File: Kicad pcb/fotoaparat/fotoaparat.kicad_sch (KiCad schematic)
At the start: 8 parts, among them J1 USB Konektor, J3 LCD konektor, J4 Kamera, J5 Sd Karta, U1 STM32L496RETx, U2 Regulator 3.3v, U3 MCP73833-FCI/UN

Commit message: První zapojení
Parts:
- added R1, R2: MCU08050D1002BP500, RESC2012X55N, symbol MCU08050D1002BP500:MCU08050D1002BP500
- added S2, S3, S4: MC32829, MC32829, symbol MC32829:MC32829
- added S5: CFS-0201MB, CFS0201MB, symbol CFS-0201MB:CFS-0201MB
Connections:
- net at U1.18 (VSS), U1.31 (VSS), U1.47 (VSS)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: now also R1.1, S5.B2 (NO_2)
- net at U1.60 (PH3): now also R1.2, S5.A1 (COM_1)
- net at U1.64 (VDD): now also R2.1, S5.B1 (NO_1)
- net at U1.7 (NRST): now also R2.2, S5.A2 (COM_2)

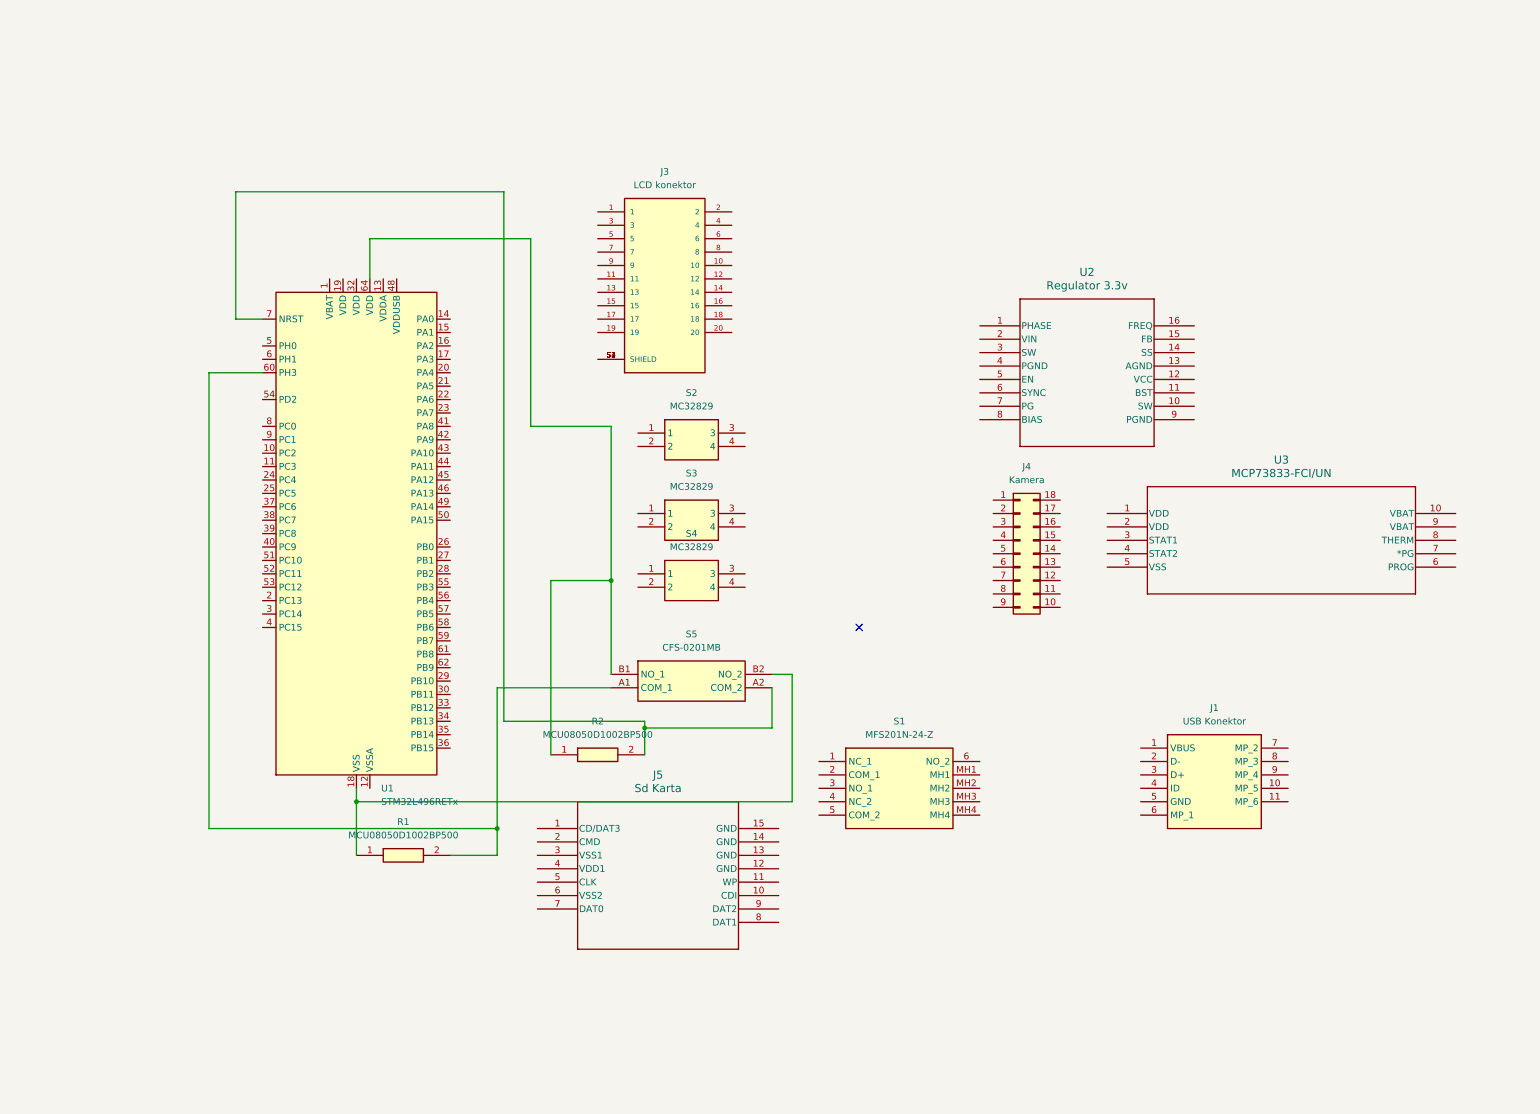
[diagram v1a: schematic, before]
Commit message: Zapojení kamery tlačítek debug pinů atd
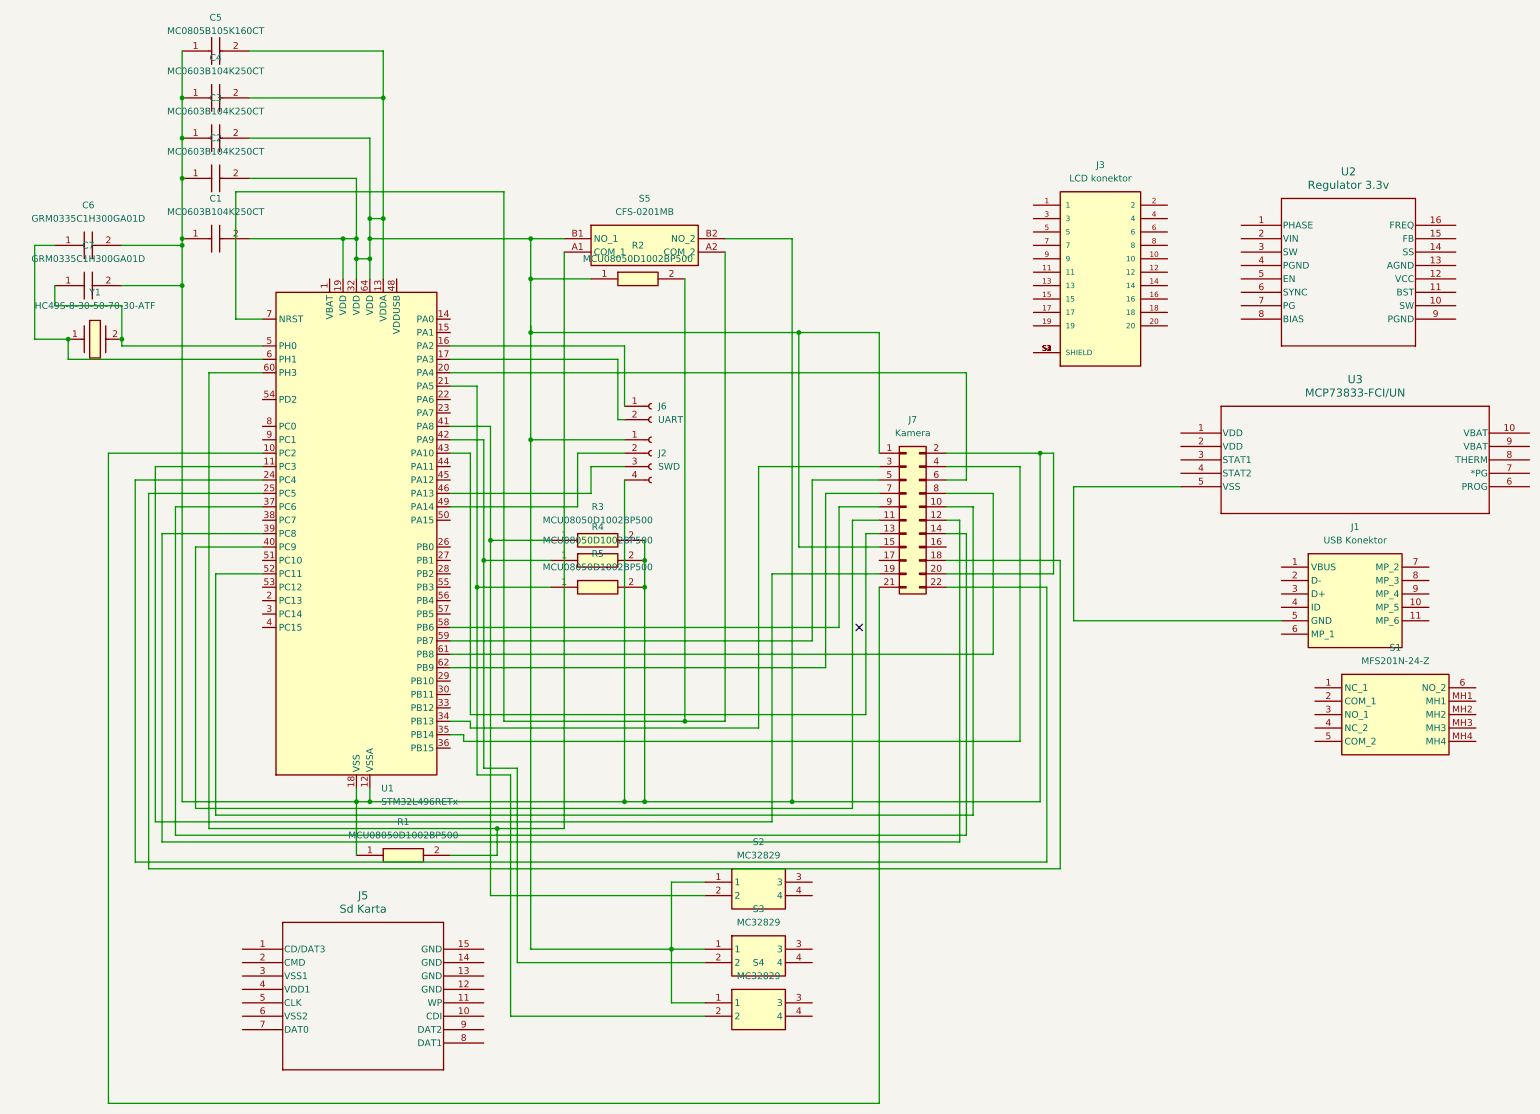
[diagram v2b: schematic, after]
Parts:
- removed J4: Kamera, Connector_PinHeader_2.54mm:PinHeader_2x09_P2.54mm_Vertical_SMD, symbol Connector_Generic:Conn_02x09_Counter_Clockwise
- added C1, C2, C3, C4: MC0603B104K250CT, mc06:CAPC1608X87N, symbol MC0603B104K250CT:MC0603B104K250CT
- added C5: MC0805B105K160CT, mc08:CAPC2012X135N, symbol MC0805B105K160CT:MC0805B105K160CT
- added C6, C7: GRM0335C1H300GA01D, grm033:GRM033D70J224ME01D, symbol GRM0335C1H300GA01D:GRM0335C1H300GA01D
- added J2: SWD, Connector_PinSocket_2.54mm:PinSocket_1x04_P2.54mm_Vertical, symbol Connector:Conn_01x04_Socket
- added J6: UART, Connector_PinSocket_2.54mm:PinSocket_1x02_P2.54mm_Vertical, symbol Connector:Conn_01x02_Socket
- added J7: Kamera, Connector_PinHeader_2.54mm:PinHeader_2x11_P2.54mm_Vertical, symbol Connector_Generic:Conn_02x11_Odd_Even
- added R3, R4, R5: MCU08050D1002BP500, 2012:RESC2012X55N, symbol MCU08050D1002BP500:MCU08050D1002BP500
- added Y1: HC49S-8-30-50-70-30-ATF, hc4:HC49S830507030ATF, symbol HC49S-8-30-50-70-30-ATF:HC49S-8-30-50-70-30-ATF
- J1: footprint 473460001 -> 47436:473460001
- J5: footprint GSD090012SEU_AMP -> gsd09:GSD090012SEU_AMP
- R1, R2: footprint RESC2012X55N -> 2012:RESC2012X55N
- S1: footprint MFS201N24Z -> mfs:MFS201N24Z
- S2, S3, S4: footprint MC32829 -> mc3:MC32829
- S5: footprint CFS0201MB -> cfs:CFS0201MB
- U2: footprint QFN-3x4_MPQ4432_MNP -> MPQ:QFN-3x4_MPQ4432_MNP
- U3: footprint MSOP10_MC_MCH -> MCP:MSOP10_MC_MCH
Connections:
- net at U1.10 (PC2): now also J7.21 (Pin_21)
- net at U1.11 (PC3): now also J7.19 (Pin_19)
- net at U1.12 (VSSA): now also R1.1, S5.B2 (NO_2), U1.18 (VSS), U1.31 (VSS), U1.47 (VSS), U1.63 (VSS), C1.1, C2.1, C3.1, C4.1, C5.1, C6.2, C7.2, J2.4 (Pin_4), J7.2 (Pin_2), J7.20 (Pin_20), R3.2, R4.2, R5.2
- net at U1.13 (VDDA): now also R2.1, S2.1, S3.1, S4.1, S5.B1 (NO_1), U1.19 (VDD), U1.32 (VDD), U1.64 (VDD), C1.2, C2.2, C3.2, C4.2, C5.2, J2.1 (Pin_1), J7.1 (Pin_1), J7.15 (Pin_15)
- net at U1.16 (PA2): now also J6.1 (Pin_1)
- net at U1.17 (PA3): now also J6.2 (Pin_2)
- net at U1.20 (PA4): now also J7.6 (Pin_6)
- net at U1.21 (PA5): now also S4.2, R5.1
- net at U1.24 (PC4): now also J7.22 (Pin_22)
- net at U1.25 (PC5): now also J7.18 (Pin_18)
- net at U1.34 (PB13): now also J7.3 (Pin_3)
- net at U1.35 (PB14): now also J7.4 (Pin_4)
- net at U1.37 (PC6): now also J7.14 (Pin_14)
- net at U1.39 (PC8): now also J7.12 (Pin_12)
- net at U1.40 (PC9): now also J7.11 (Pin_11)
- net at U1.41 (PA8): now also S2.2, R3.1
- net at U1.42 (PA9): now also S3.2, R4.1
- net at U1.43 (PA10): now also J7.13 (Pin_13)
- net at U1.46 (PA13): now also J2.3 (Pin_3)
- net at U1.49 (PA14): now also J2.2 (Pin_2)
- net at U1.5 (PH0): now also C7.1, Y1.2
- net at U1.52 (PC11): now also J7.10 (Pin_10)
- net at U1.58 (PB6): now also J7.9 (Pin_9)
- net at U1.59 (PB7): now also J7.5 (Pin_5)
- net at U1.6 (PH1): now also C6.1, Y1.1
- net at U1.61 (PB8): now also J7.8 (Pin_8)
- net at U1.62 (PB9): now also J7.7 (Pin_7)
- net at U3.5 (VSS): now also J1.5 (GND)
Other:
- moved on the sheet: J1, J3, J5, R2, S1, S2, S3, S4, S5, U2, U3

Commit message: Lcd Konektor
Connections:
- net at C1.2, C2.2, C3.2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: now also J3.2, J3.5
- net at C1.1, C2.1, C3.1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: now also J3.1, J3.11, J3.20, J3.3, J3.4
- net at U1.15 (PA1): now also J3.8
- net at U1.22 (PA6): now also J3.12
- net at U1.23 (PA7): now also J3.7

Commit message: Baterie
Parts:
- added C8: MC0603B104K250CT, mc06:CAPC1608X87N, symbol MC0603B104K250CT:MC0603B104K250CT
- added J4: Baterie, symbol Connector:Conn_01x02_Socket
- added R10, R6, R7, R8, R9: MCU08050D1002BP500, 2012:RESC2012X55N, symbol MCU08050D1002BP500:MCU08050D1002BP500
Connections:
- net at S1.MH1: now also C1.1, C2.1, C3.1, C4.1, C5.1, C6.2, C7.2, J1.10 (MP_5), J1.11 (MP_6), J1.5 (GND), J1.6 (MP_1), J1.7 (MP_2), J1.8 (MP_3), J1.9 (MP_4), J2.4 (Pin_4), J3.1, J3.11, J3.15, J3.20, J3.3, J3.4, J3.S1 (SHIELD), J3.S2 (SHIELD), J3.S3 (SHIELD), J3.S4 (SHIELD), J5.12 (GND), J5.13 (GND), J5.14 (GND), J5.15 (GND), J5.3 (VSS1), J5.6 (VSS2), J7.2 (Pin_2), J7.20 (Pin_20), R1.1, R3.2, R4.2, R5.2, S1.MH2, S1.MH3, S1.MH4, S5.B2 (NO_2), U1.12 (VSSA), U1.18 (VSS), U1.31 (VSS), U1.47 (VSS), U1.63 (VSS), U3.5 (VSS), C8.2, J4.1 (Pin_1), R10.1
- net at C1.2, C2.2, C3.2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: now also J3.14, J5.4 (VDD1), C8.1, R6.1, R7.1, R8.1
- net at J7.21 (Pin_21): now also U1.9 (PC1); no longer U1.10 (PC2)
- net at U1.26 (PB0): now also J3.9
- net at U1.27 (PB1): now also J3.10
- net at U1.29 (PB10): now also J5.5 (CLK)
- net at U1.33 (PB12): now also J5.1 (CD/DAT3), R1.2, S5.A1 (COM_1), U1.60 (PH3), R6.2
- net at U1.36 (PB15): now also J5.2 (CMD), R8.2
- net at U1.44 (PA11): now also J3.6
- net at U1.8 (PC0): now also R10.2, R9.1
- net at J5.7 (DAT0): now also U1.10 (PC2), R7.2
- net at U3.10 (VBAT): now also J4.2 (Pin_2), R9.2
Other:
- moved on the sheet: J1, S1, U2, U3

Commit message: Přepojení součástek
vypadá to trochu lépe
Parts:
- removed C1, C2, C3, C4, C8: MC0603B104K250CT, mc06:CAPC1608X87N, symbol MC0603B104K250CT:MC0603B104K250CT
- removed C5: MC0805B105K160CT, mc08:CAPC2012X135N, symbol MC0805B105K160CT:MC0805B105K160CT
- removed C6, C7: GRM0335C1H300GA01D, grm033:GRM033D70J224ME01D, symbol GRM0335C1H300GA01D:GRM0335C1H300GA01D
- removed R1, R10, R2, R3, R4, R5, R6, R7, R8, R9: MCU08050D1002BP500, 2012:RESC2012X55N, symbol MCU08050D1002BP500:MCU08050D1002BP500
- removed U2: Regulator 3.3v, MPQ:QFN-3x4_MPQ4432_MNP, symbol 2025-09-30_17-10-32:MPQ4432GL-AEC1-P
- added C10, C11, C12, C9: 100n, Capacitor_SMD:C_0603_1608Metric_Pad1.08x0.95mm_HandSolder, symbol Device:C
- added C13: 5u, symbol Device:C
- added C14: 10n, Capacitor_SMD:C_0603_1608Metric_Pad1.08x0.95mm_HandSolder, symbol Device:C
- added C15, C16: 1u, symbol Device:C
- added C17, C18: 30p, Capacitor_SMD:C_0201_0603Metric_Pad0.64x0.40mm_HandSolder, symbol Device:C
- added FB1: 120R, symbol Device:FerriteBead
- added IC1: NCP718ASN330T1G, SOT95P280X100-5N, symbol NCP718ASN330T1G:NCP718ASN330T1G
- added R1, R11, R12, R13, R2, R3: 1.5k, symbol Device:R
- S2: value MC32829 -> tlačítko doleva
- S3: value MC32829 -> prostřední tlačítko
- S4: value MC32829 -> tlačítko doprava
- S5: value CFS-0201MB -> spínač
- Y1: value HC49S-8-30-50-70-30-ATF -> 8mhz krystal
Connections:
- net at J4.2 (Pin_2): no longer U3.10 (VBAT)
- net +3.3V: now reaches J2.1 (Pin_1), J3.2, J3.5, J7.1 (Pin_1), J7.15 (Pin_15), U1.19 (VDD), U1.32 (VDD), U1.64 (VDD)
- net +3.3V: now also J5.3 (VSS1), J5.6 (VSS2), S5.A2 (COM_2), U1.1 (VBAT), C10.2, C11.2, C12.2, C13.2, C16.1, C9.2, FB1.2, R1.1, R11.1, R13.2, R2.1, R3.1; no longer J3.14, J5.4 (VDD1), S2.1, S3.1, S4.1, S5.B1 (NO_1), U1.13 (VDDA)
- net d4: now reaches J7.10 (Pin_10), U1.52 (PC11)
- net d3: now reaches J7.11 (Pin_11), U1.40 (PC9)
- net d2: now reaches J7.12 (Pin_12), U1.39 (PC8)
- net at U1.43 (PA10): no longer J7.13 (Pin_13)
- net d0: now reaches J7.14 (Pin_14), U1.37 (PC6)
- net rck: now reaches J7.18 (Pin_18)
- net rck: now also U1.53 (PC12); no longer U1.25 (PC5)
- net sw1: now reaches U1.11 (PC3)
- net sw1: now also S2.4, R3.2; no longer J7.19 (Pin_19)
- net sda: now reaches U1.9 (PC1)
- net sda: now also J3.7, J7.4 (Pin_4), U1.30 (PB11); no longer J7.21 (Pin_21)
- net rrst: now reaches J7.22 (Pin_22)
- net rrst: now also U1.2 (PC13); no longer U1.24 (PC4)
- net scl: now reaches J7.3 (Pin_3), U1.34 (PB13)
- net scl: now also J3.8, U1.29 (PB10)
- net at U1.35 (PB14): no longer J7.4 (Pin_4)
- net vsync: now reaches J7.5 (Pin_5), U1.59 (PB7)
- net href: now reaches J7.6 (Pin_6), U1.20 (PA4)
- net d7: now reaches J7.7 (Pin_7), U1.62 (PB9)
- net d6: now reaches J7.8 (Pin_8), U1.61 (PB8)
- net d5: now reaches J7.9 (Pin_9), U1.58 (PB6)
- net sd miso: now reaches J5.7 (DAT0)
- net sd miso: now also U1.56 (PB4); no longer U1.10 (PC2)
- net uart tx: now reaches U1.14 (PA0)
- net uart tx: now also J6.1 (Pin_1)
- net uart rx: now reaches U1.15 (PA1)
- net uart rx: now also J6.2 (Pin_2); no longer J3.8
- net at U1.16 (PA2): no longer J6.1 (Pin_1)
- net sd cs: now reaches U1.17 (PA3)
- net sd cs: now also J5.1 (CD/DAT3); no longer J6.2 (Pin_2)
- net at S4.2: no longer U1.21 (PA5)
- net sdo: now reaches J3.12
- net sdo: now also U1.10 (PC2); no longer U1.22 (PA6)
- net sd mosi: now reaches U1.23 (PA7)
- net sd mosi: now also J5.2 (CMD); no longer J3.7
- net at U1.26 (PB0): no longer J3.9
- net at U1.27 (PB1): no longer J3.10
- net sd clk: now reaches J5.5 (CLK)
- net sd clk: now also U1.21 (PA5); no longer U1.29 (PB10)
- net wrst: now reaches U1.3 (PC14)
- net wrst: now also J7.21 (Pin_21)
- net at U1.36 (PB15): no longer J5.2 (CMD)
- net d1: now reaches U1.38 (PC7)
- net d1: now also J7.13 (Pin_13)
- net at U1.41 (PA8): no longer S2.2
- net at U1.42 (PA9): no longer S3.2
- net at J3.6: no longer U1.44 (PA11)
- net data +: now reaches U1.45 (PA12)
- net data +: now also J1.3 (D+)
- net swclk: now reaches J2.3 (Pin_3)
- net swclk: now also U1.49 (PA14); no longer U1.46 (PA13)
- net +3.3VA: now reaches U1.48 (VDDUSB)
- net +3.3VA: now also C14.1, C15.1, FB1.1
- net swdio: now reaches J2.2 (Pin_2)
- net swdio: now also U1.46 (PA13); no longer U1.49 (PA14)
- net osc in: now reaches U1.5 (PH0)
- net osc in: now also Y1.1, C17.2; no longer Y1.2
- net osc out: now reaches U1.6 (PH1)
- net osc out: now also Y1.2, C18.2; no longer Y1.1
- net Reset: now reaches U1.7 (NRST)
- net Reset: now also S5.A1 (COM_1), R11.2; no longer S5.A2 (COM_2)
- net GND: now reaches S4.3
- net GND: now also J1.5 (GND), J2.4 (Pin_4), J3.1, J3.11, J3.15, J3.20, J3.3, J3.4, J5.4 (VDD1), J7.2 (Pin_2), J7.20 (Pin_20), S2.3, S3.3, S5.B1 (NO_1), U1.12 (VSSA), U1.18 (VSS), U1.31 (VSS), U1.47 (VSS), U1.63 (VSS), C10.1, C11.1, C12.1, C13.1, C14.2, C15.2, C16.2, C17.1, C18.1, C9.1, R12.1
- net sw3: now reaches S4.4
- net sw3: now also U1.25 (PC5), R1.2
- net sw2: now reaches S3.4
- net sw2: now also U1.24 (PC4), R2.2
- net VBUS: now reaches J1.1 (VBUS)
- net data -: now reaches J1.2 (D-)
- net data -: now also U1.44 (PA11)
- new net: J3.14, R13.1
- new net: J3.S1 (SHIELD), J3.S2 (SHIELD), J3.S3 (SHIELD), J3.S4 (SHIELD)
- new net boot0: R12.2, S5.B2 (NO_2), U1.60 (PH3)
- new net wr: J7.19 (Pin_19), U1.22 (PA6)
- now unconnected: J1.10 (MP_5), J1.11 (MP_6), J1.6 (MP_1), J1.7 (MP_2), J1.8 (MP_3), J1.9 (MP_4), J4.1 (Pin_1), J5.12 (GND), J5.13 (GND), J5.14 (GND), J5.15 (GND), S1.MH1, S1.MH2, S1.MH3, S1.MH4, U1.33 (PB12), U3.5 (VSS)
- no-connect marks 1 -> 29
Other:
- moved on the sheet: J1, J2, J3, J4, J5, J6, J7, S1, S2, S3, S4, S5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

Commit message: Baterie nabíječka
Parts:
- added C1, C2: 1u, symbol Device:C
- added D1, D2, D3: LED, symbol Device:LED
- added R4, R5, R6: 1.5k, symbol Device:R
- added R7: 1k, symbol Device:R
- added TH1: 10k, symbol Device:Thermistor
- IC1: value NCP718ASN330T1G -> Lineární Regulátor
- S1: value MFS201N-24-Z -> Zapínací spínač
- U3: value MCP73833-FCI/UN -> Nabíječka baterie
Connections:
- net GND is gone; now on net -BATT: C10.1, C11.1, C12.1, C13.1, C14.2, C15.2, C16.2, C17.1, C18.1, C9.1, J1.5 (GND), J2.4 (Pin_4), J3.1, J3.11, J3.15, J3.20, J3.3, J3.4, J5.4 (VDD1), J7.2 (Pin_2), J7.20 (Pin_20), R12.1, S2.3, S3.3, S4.3, S5.B1 (NO_1), U1.12 (VSSA), U1.18 (VSS), U1.31 (VSS), U1.47 (VSS), U1.63 (VSS)
- net VBUS: now also U3.1 (VDD), U3.2 (VDD), C1.1, D1.2 (A), D2.2 (A), D3.2 (A)
- net +BATT: now reaches J4.1 (Pin_1)
- net +BATT: now also U3.10 (VBAT), U3.9 (VBAT), C2.1
- net -BATT: now reaches J4.2 (Pin_2)
- net -BATT: now also U3.5 (VSS), C1.2, C2.2, R7.2, TH1.2
- net at U3.3 (STAT1): now also R4.2
- net at U3.4 (STAT2): now also R5.2
- net at U3.6 (PROG): now also R7.1
- net at U3.7 (*PG): now also R6.2
- net at U3.8 (THERM): now also TH1.1
- new net: D2.1 (K), R5.1
- new net: D1.1 (K), R4.1
- new net Indikátor Nabíjení: D3.1 (K), R6.1
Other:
- moved on the sheet: IC1, J4, S1, U3

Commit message: Regulátory
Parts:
- added C19, C20, C3, C4, C5, C6, C7, C8: 1u, Capacitor_SMD:C_0805_2012Metric_Pad1.18x1.45mm_HandSolder, symbol Device:C
- added IC2: Lineární Regulátor Displaye, Package_TO_SOT_SMD:TSOT-23-5_HandSoldering, symbol NCP718ASN330T1G:NCP718ASN330T1G
- added R10, R14, R15, R16, R17, R18, R19, R20, R21, R22, R23, R24, R9: 4.7k, Resistor_SMD:R_0805_2012Metric_Pad1.20x1.40mm_HandSolder, symbol Device:R
- added R8: 2, Resistor_SMD:R_0805_2012Metric_Pad1.20x1.40mm_HandSolder, symbol Device:R
- C1, C15, C16, C2: footprint (none) -> Capacitor_SMD:C_0805_2012Metric_Pad1.18x1.45mm_HandSolder
- C10, C11, C12, C9: footprint Capacitor_SMD:C_0603_1608Metric_Pad1.08x0.95mm_HandSolder -> Capacitor_SMD:C_0805_2012Metric_Pad1.18x1.45mm_HandSolder
- C13: value 5u -> 1u; footprint (none) -> Capacitor_SMD:C_0805_2012Metric_Pad1.18x1.45mm_HandSolder
- C14: value 10n -> 100n; footprint Capacitor_SMD:C_0603_1608Metric_Pad1.08x0.95mm_HandSolder -> Capacitor_SMD:C_0805_2012Metric_Pad1.18x1.45mm_HandSolder
- C17, C18: footprint Capacitor_SMD:C_0201_0603Metric_Pad0.64x0.40mm_HandSolder -> Capacitor_SMD:C_0805_2012Metric_Pad1.18x1.45mm_HandSolder
- D1, D2, D3: footprint (none) -> LED_SMD:LED_0805_2012Metric_Pad1.15x1.40mm_HandSolder
- FB1: footprint (none) -> Inductor_SMD:L_0805_2012Metric_Pad1.05x1.20mm_HandSolder
- IC1: footprint SOT95P280X100-5N -> Package_TO_SOT_SMD:TSOT-23-5_HandSoldering
- J2: footprint Connector_PinSocket_2.54mm:PinSocket_1x04_P2.54mm_Vertical -> Connector_PinHeader_2.54mm:PinHeader_1x04_P2.54mm_Vertical
- J4, TH1: footprint (none) -> Connector_PinSocket_2.54mm:PinSocket_1x02_P2.54mm_Horizontal
- J6: footprint Connector_PinSocket_2.54mm:PinSocket_1x02_P2.54mm_Vertical -> Connector_PinHeader_2.54mm:PinHeader_1x02_P2.54mm_Vertical
- J7: footprint Connector_PinHeader_2.54mm:PinHeader_2x11_P2.54mm_Vertical -> Connector_PinSocket_2.54mm:PinSocket_2x11_P2.54mm_Vertical
- R1, R11, R12, R13, R2, R3: value 1.5k -> 4.7k; footprint (none) -> Resistor_SMD:R_0805_2012Metric_Pad1.20x1.40mm_HandSolder
- R4, R5, R6: value 1.5k -> 1k; footprint (none) -> Resistor_SMD:R_0805_2012Metric_Pad1.20x1.40mm_HandSolder
- R7: footprint (none) -> Resistor_SMD:R_0805_2012Metric_Pad1.20x1.40mm_HandSolder
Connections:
- net +3.3V: now also IC1.5 (OUT), C19.2, C20.2, C4.2, C7.2, C8.2, R10.1, R15.1, R18.1, R21.1, R9.1; no longer J3.2, J3.5, R13.2
- net +BATT: now also IC1.1 (IN), S1.2 (COM_1), C3.1, C5.1, IC2.1 (IN)
- net -BATT: now also IC1.2 (GND), C19.1, C20.1, C3.2, C4.1, C5.2, C6.1, C7.1, C8.1, IC2.2 (GND), R14.1, R24.1
- net scl: now also R9.2
- net sd cs: now also R17.2
- net sd miso: now also R23.2
- net sd mosi: now also R20.2
- net sdo: now also J7.4 (Pin_4), U1.30 (PB11), R10.2
- net at S1.3 (NO_1): now also IC1.3 (EN), R24.2
- net Backlight Regulátor: now reaches S1.5 (COM_2)
- net Backlight Regulátor: now also U1.4 (PC15)
- net at S1.6 (NO_2): now also IC2.3 (EN), R14.2
- net rst: now reaches U1.28 (PB2)
- net rst: now also J3.6
- net csx: now reaches U1.55 (PB3)
- net csx: now also J3.7, J3.9, U1.9 (PC1)
- net wrx d/cx: now reaches U1.57 (PB5)
- net wrx d/cx: now also J3.10
- net data + renamed USB_D+
- net data - renamed USB_D-
- removed net sda: J3.7, J7.4 (Pin_4), U1.30 (PB11), U1.9 (PC1)
- new net: R18.2, R19.1
- new net: R15.2, R16.1
- new net: R19.2, R20.1
- new net: J3.2, R8.2
- new net: R21.2, R22.1
- new net: R22.2, R23.1
- new net: R16.2, R17.1
- new net +3.3V LCD: C6.2, IC2.5 (OUT), J3.5, R13.2, R8.1
- no-connect marks 29 -> 37
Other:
- note added: "Regulátory"
- note added: "Stm32 mikrokontrolér"
- company: (none) -> Vilem Maly
- title: (none) -> Stm32 Fotoaparát
- moved on the sheet: IC1, S1
